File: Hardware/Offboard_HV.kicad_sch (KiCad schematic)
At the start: 9 parts, among them J3 ICM-20948, SW1 SW_START, SW3 SW_DIRECTION, SW4 SW_BRAKE, SW5 SW_PUSH_EMERGENCY_NO, SW6 SW_PUSH_EMERGENCY_NC

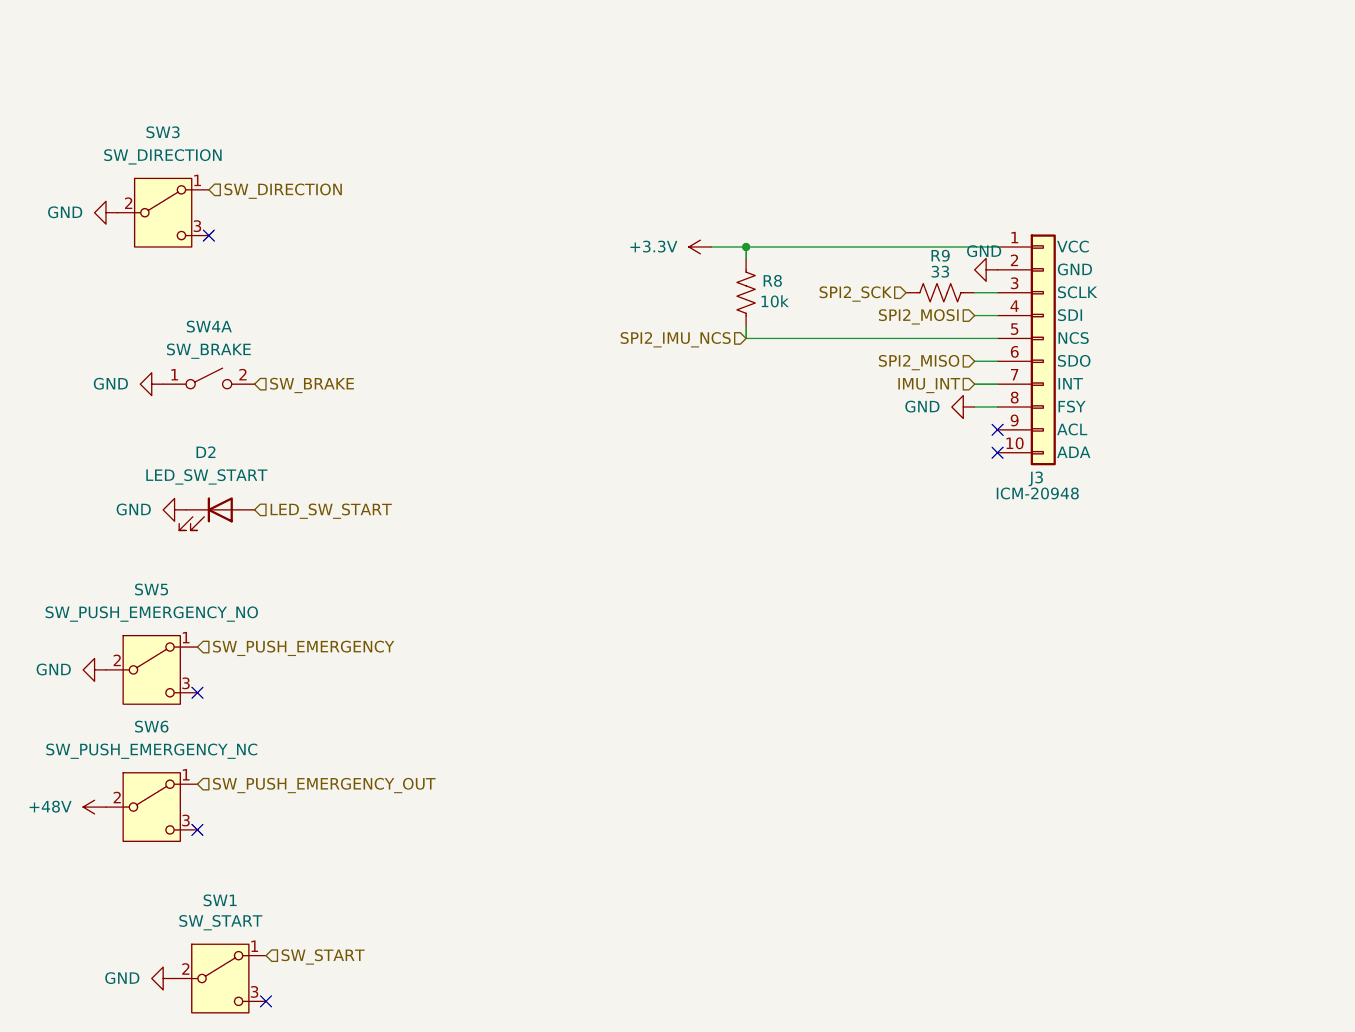
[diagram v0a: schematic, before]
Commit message: Restructure VCU schema
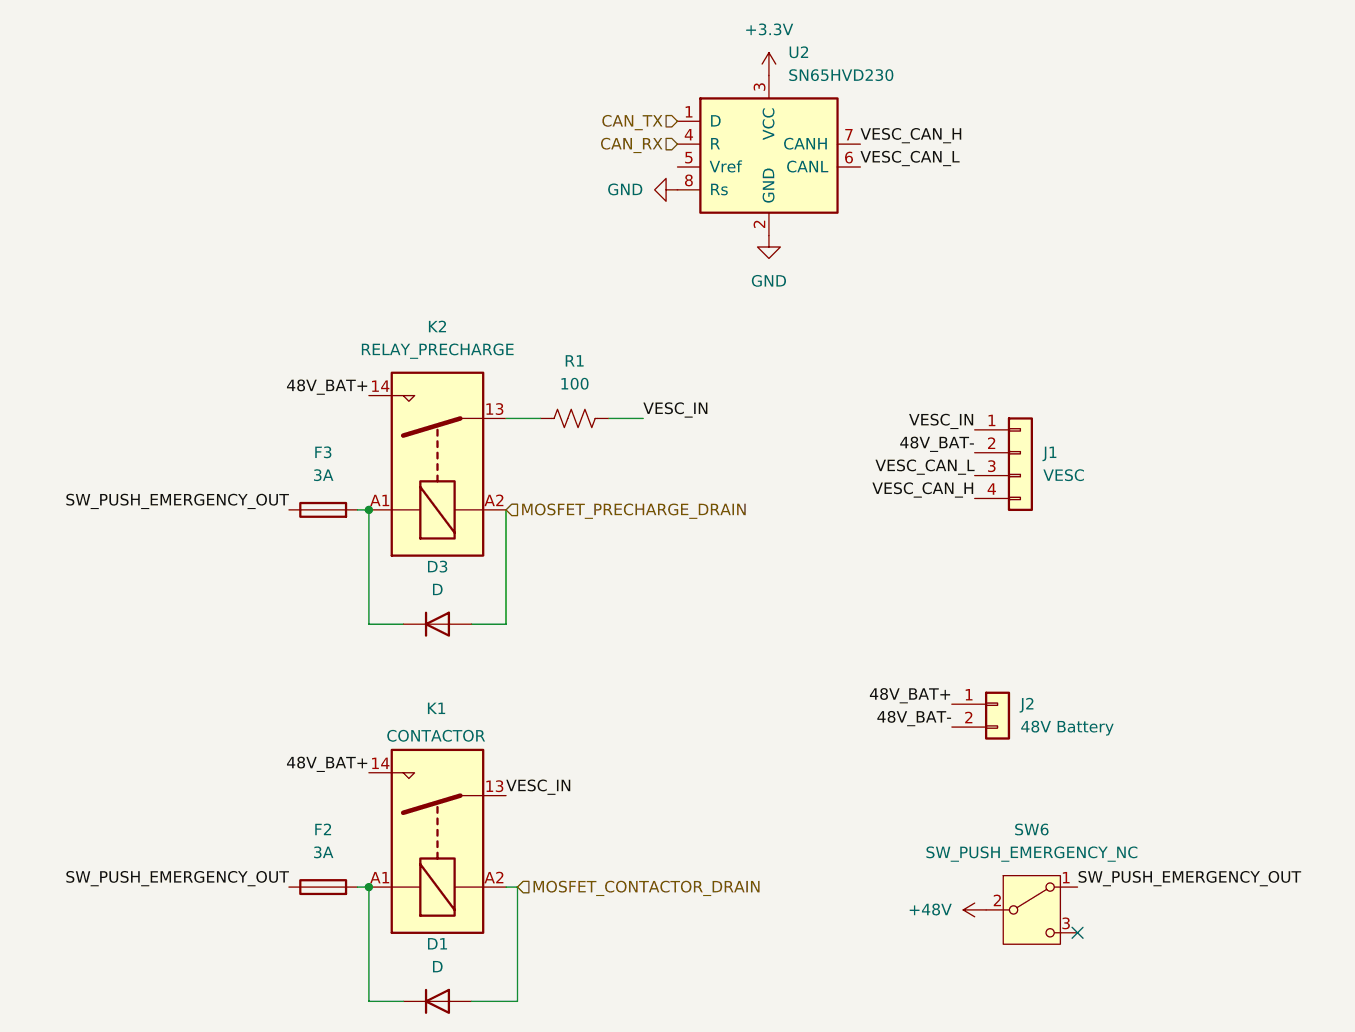
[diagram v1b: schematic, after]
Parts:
- removed D2: LED_SW_START, Package_SON:WSON-8-1EP_6x5mm_P1.27mm_EP3.4x4mm, symbol Device:LED
- removed J3: ICM-20948, Package_DFN_QFN:QFN-20-1EP_5x5mm_P0.65mm_EP3.35x3.35mm, symbol Connector_Generic:Conn_01x10
- removed R8: 10k, Resistor_THT:R_Array_SIP4, symbol Device:R_US
- removed R9: 33, symbol Device:R_US
- removed SW1: SW_START, Button_Switch_SMD:Nidec_Copal_CAS-120A, symbol Switch:SW_SPDT
- removed SW3: SW_DIRECTION, Module:RaspberryPi_Pico_W_SMD_HandSolder, symbol Switch:SW_SPDT
- removed SW4: SW_BRAKE, Button_Switch_THT:SW_NKK_GW12LJP, symbol Switch:SW_DPST_x2
- removed SW5: SW_PUSH_EMERGENCY_NO, Module:RaspberryPi_Pico_W_SMD_HandSolder, symbol Switch:SW_SPDT
- added D1, D3: D, symbol Device:D
- added F2, F3: 3A, symbol Device:Fuse
- added J1: VESC, symbol Connector_Generic:Conn_01x04
- added J2: 48V Battery, symbol Connector_Generic:Conn_01x02
- added K1: CONTACTOR, Relay_THT:Relay_NCR_HHG1D-1, symbol Relay:Relay_SPST-NO
- added K2: RELAY_PRECHARGE, Relay_THT:Relay_NCR_HHG1D-1, symbol Relay:Relay_SPST-NO
- added R1: 100, symbol Device:R_US
- added U2: SN65HVD230, Package_SO:SOIC-8_3.9x4.9mm_P1.27mm, symbol Interface_CAN_LIN:SN65HVD230
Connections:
- net +3.3V: now also U2.3 (VCC)
- net GND: now also U2.2 (GND), U2.8 (Rs)
- net SW_PUSH_EMERGENCY_OUT: now also F2.1, F3.1
- new net: D3.1 (K), F3.2, K2.A1
- new net: D1.1 (K), F2.2, K1.A1
- new net: K2.13, R1.1
- new net 48V_BAT+: J2.1 (Pin_1), K1.14, K2.14
- new net 48V_BAT-: J1.2 (V-), J2.2 (Pin_2)
- new net CAN_RX: U2.4 (R)
- new net CAN_TX: U2.1 (D)
- new net MOSFET_CONTACTOR_DRAIN: D1.2 (A), K1.A2
- new net MOSFET_PRECHARGE_DRAIN: D3.2 (A), K2.A2
- new net VESC_CAN_H: J1.4 (CAN_H), U2.7 (CANH)
- new net VESC_CAN_L: J1.3 (CAN_L), U2.6 (CANL)
- new net VESC_IN: J1.1 (V+), K1.13, R1.2
- no-connect marks 6 -> 1

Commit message: Set footprint + excludes
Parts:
- R1: footprint (none) -> Resistor_THT:R_Axial_DIN0207_L6.3mm_D2.5mm_P7.62mm_Horizontal
- SW6: now left out of the parts list
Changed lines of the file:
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@@
 		(body_style 1)
 		(exclude_from_sim no)
-		(in_bom yes)
-		(on_board yes)
+		(in_bom no)
+		(on_board no)
 		(in_pos_files yes)
 		(dnp no)
@@
 			)
 		)
-		(property "Footprint" ""
+		(property "Footprint" "Resistor_THT:R_Axial_DIN0207_L6.3mm_D2.5mm_P7.62mm_Horizontal"
 			(at 122.174 85.344 90)
 			(hide yes)
